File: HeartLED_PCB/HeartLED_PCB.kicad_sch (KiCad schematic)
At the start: 36 parts, among them U1 ICM7555CBAZ, U2 CD4017BM, U3 HT7750A, U4 HX SS12F44G4

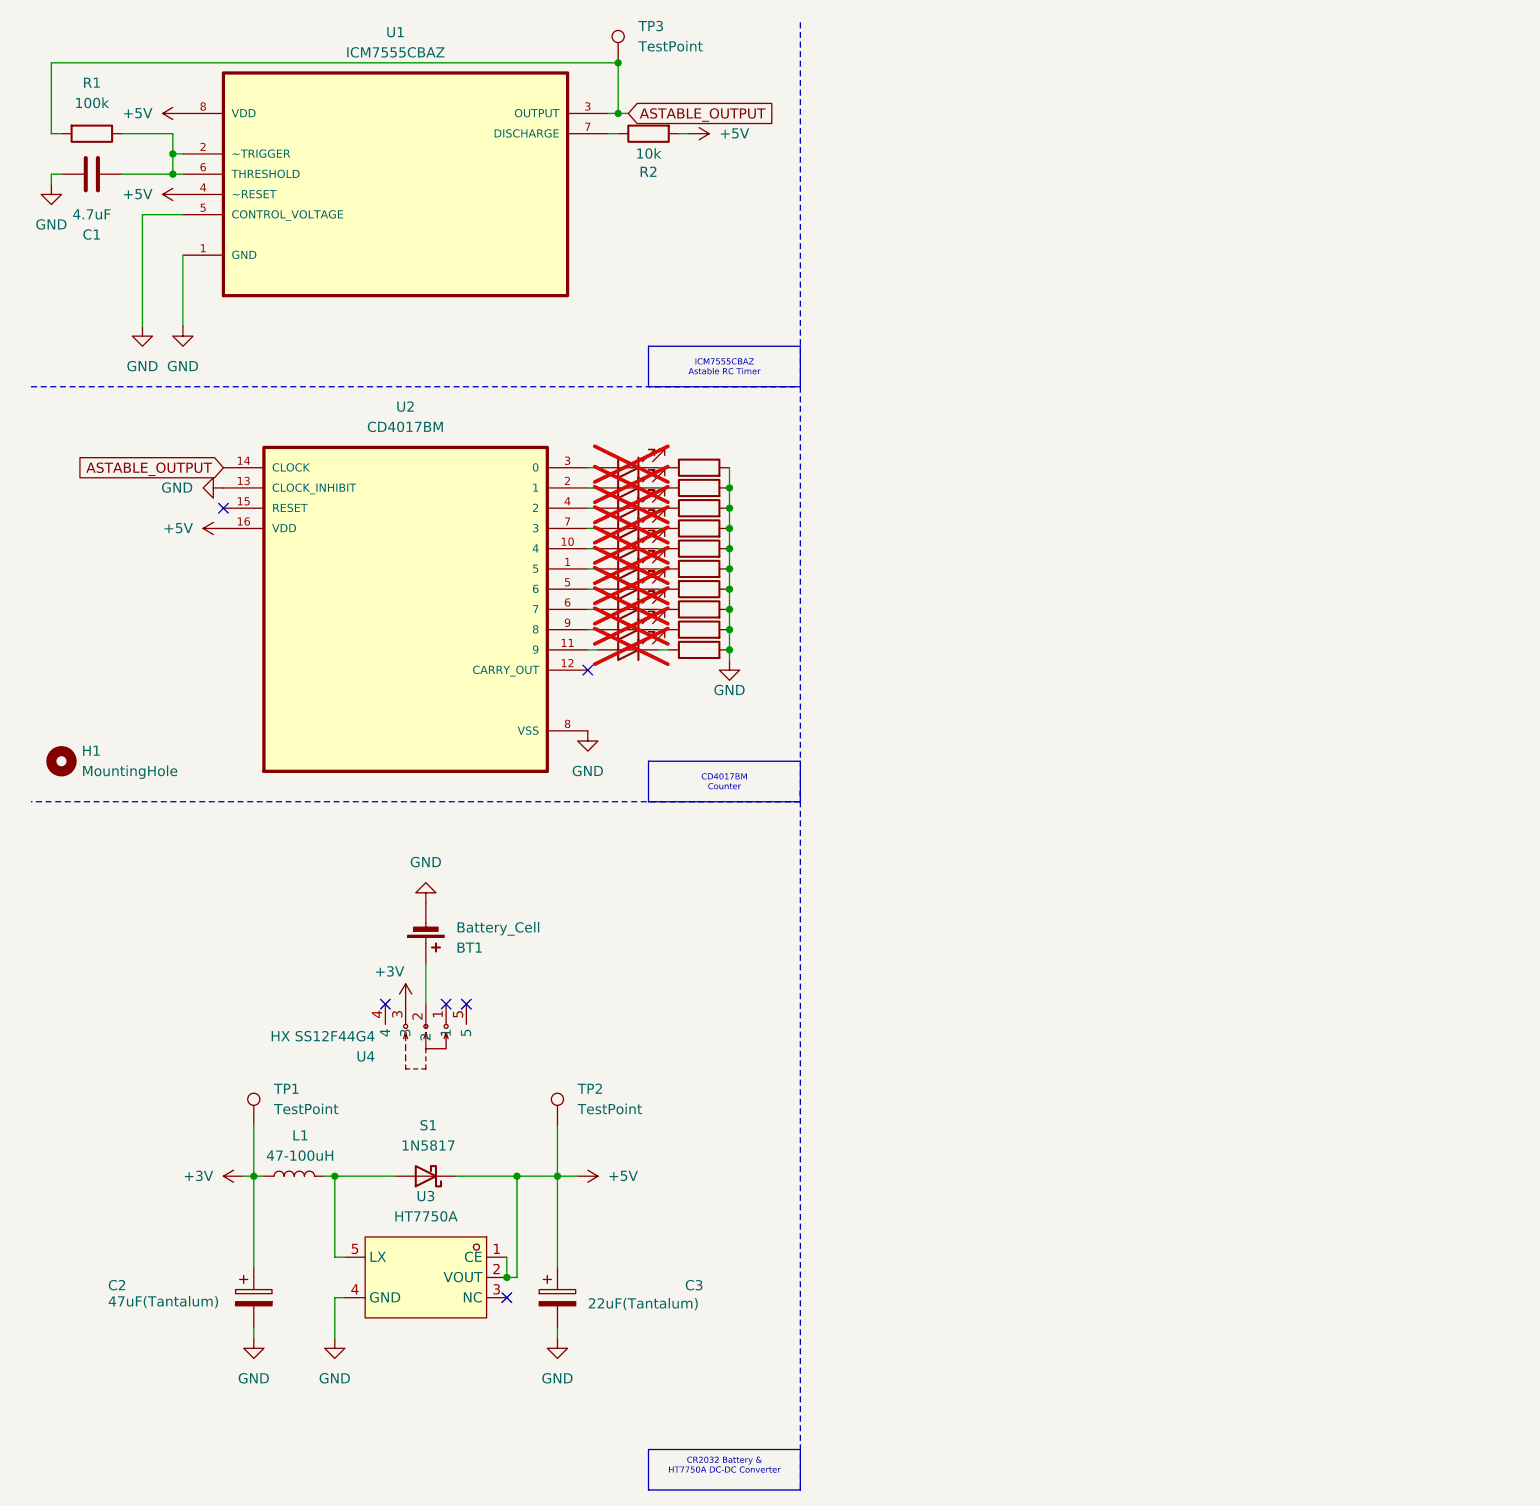
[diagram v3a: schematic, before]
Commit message: Changed Timer and Counter models
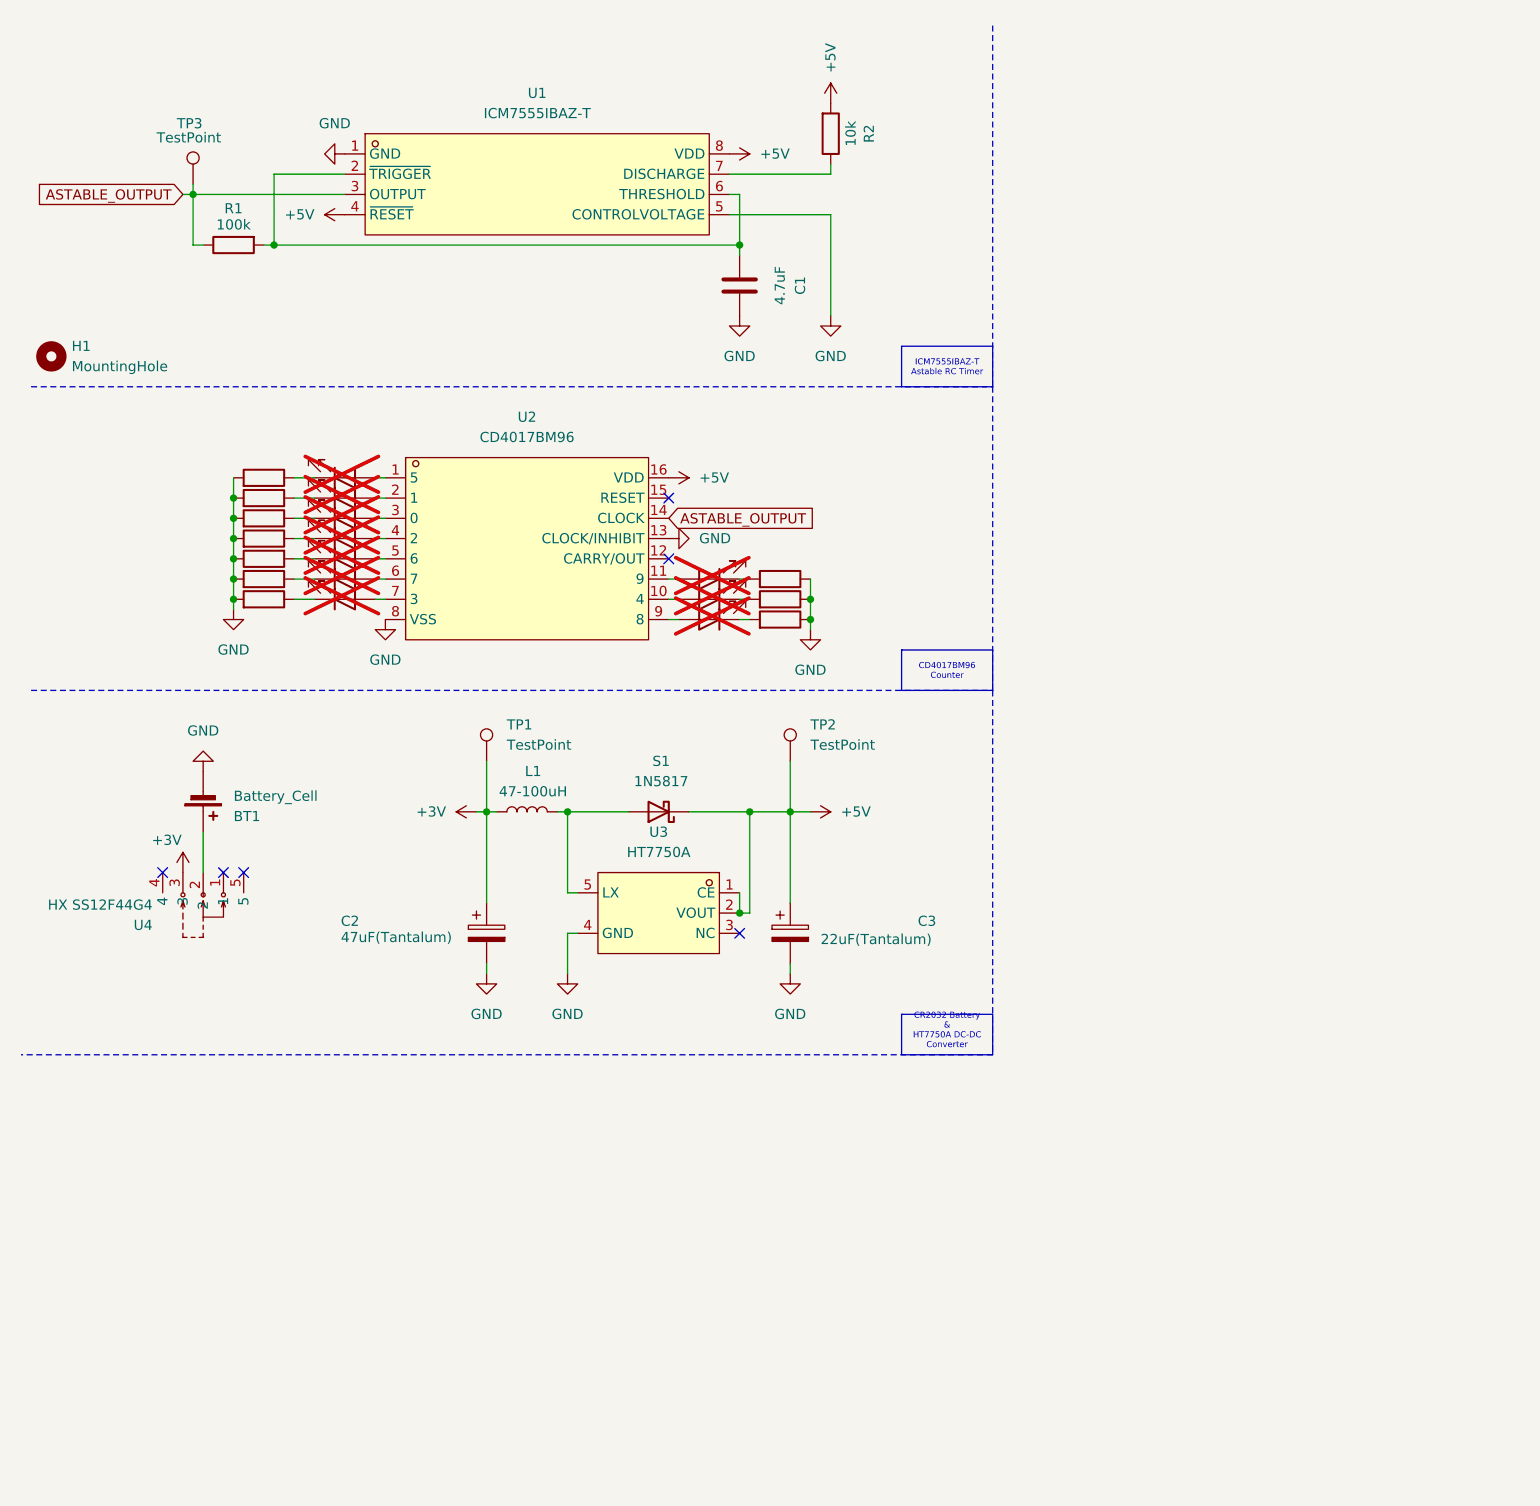
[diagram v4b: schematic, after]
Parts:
- removed U1: ICM7555CBAZ, FOOTPRINTS:ICM7555CBAZ, symbol ICM7555CBAZ:ICM7555CBAZ
- removed U2: CD4017BM, FOOTPRINTS:CD4017BM, symbol CD4017BM:CD4017BM
- added U1: ICM7555IBAZ-T, FOOTPRINTS:ICM7555IBAZ-T, symbol ICM7555IBAZ-T:ICM7555IBAZ-T
- added U2: CD4017BM96, FOOTPRINTS:CD4017BM96, symbol CD4017BM96:CD4017BM96
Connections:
- net +5V: now also U1.4 (~{RESET}), U1.8 (VDD), U2.16 (VDD)
- net ASTABLE_OUTPUT: now also R1.1, U1.3 (OUTPUT), U2.14 (CLOCK); no longer R1.2
- net GND: now also R10.1, R11.1, R12.1, U1.1 (GND), U1.5 (CONTROLVOLTAGE), U2.13 (CLOCK/INHIBIT), U2.8 (VSS); no longer R10.2, R11.2, R12.2
- net at D9.1 (K): now also R11.2; no longer R11.1
- net at D10.1 (K): now also R12.2; no longer R12.1
- net at D8.1 (K): now also R10.2; no longer R10.1
- net at D1.2 (A): now also U2.1 (5)
- net at D10.2 (A): now also U2.11 (9)
- net at C1.1: now also R1.2, U1.2 (~{TRIGGER}), U1.6 (THRESHOLD); no longer R1.1
- net at R2.1: now also U1.7 (DISCHARGE)
- net at D3.2 (A): now also U2.3 (0)
- net at D8.2 (A): now also U2.9 (8)
- net at D9.2 (A): now also U2.10 (4)
- net at D2.2 (A): now also U2.2 (1)
- net at D4.2 (A): now also U2.4 (2)
- net at D5.2 (A): now also U2.5 (6)
- net at D6.2 (A): now also U2.6 (7)
- net at D7.2 (A): now also U2.7 (3)
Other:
- moved on the sheet: BT1, C1, C2, C3, H1, L1, R1, R2, S1, TP1, TP2, TP3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

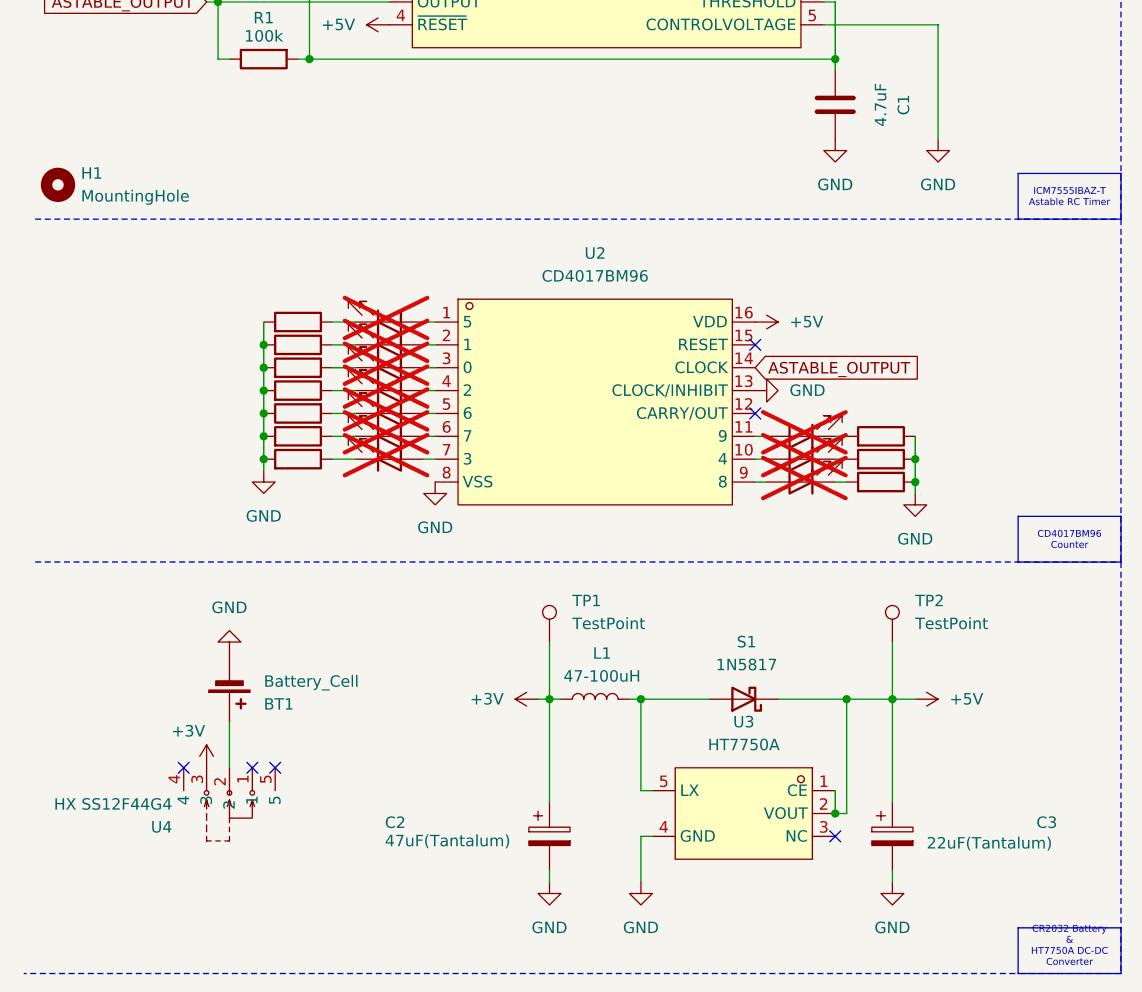
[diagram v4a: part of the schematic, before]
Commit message: Changed DC-DC Boost Converter
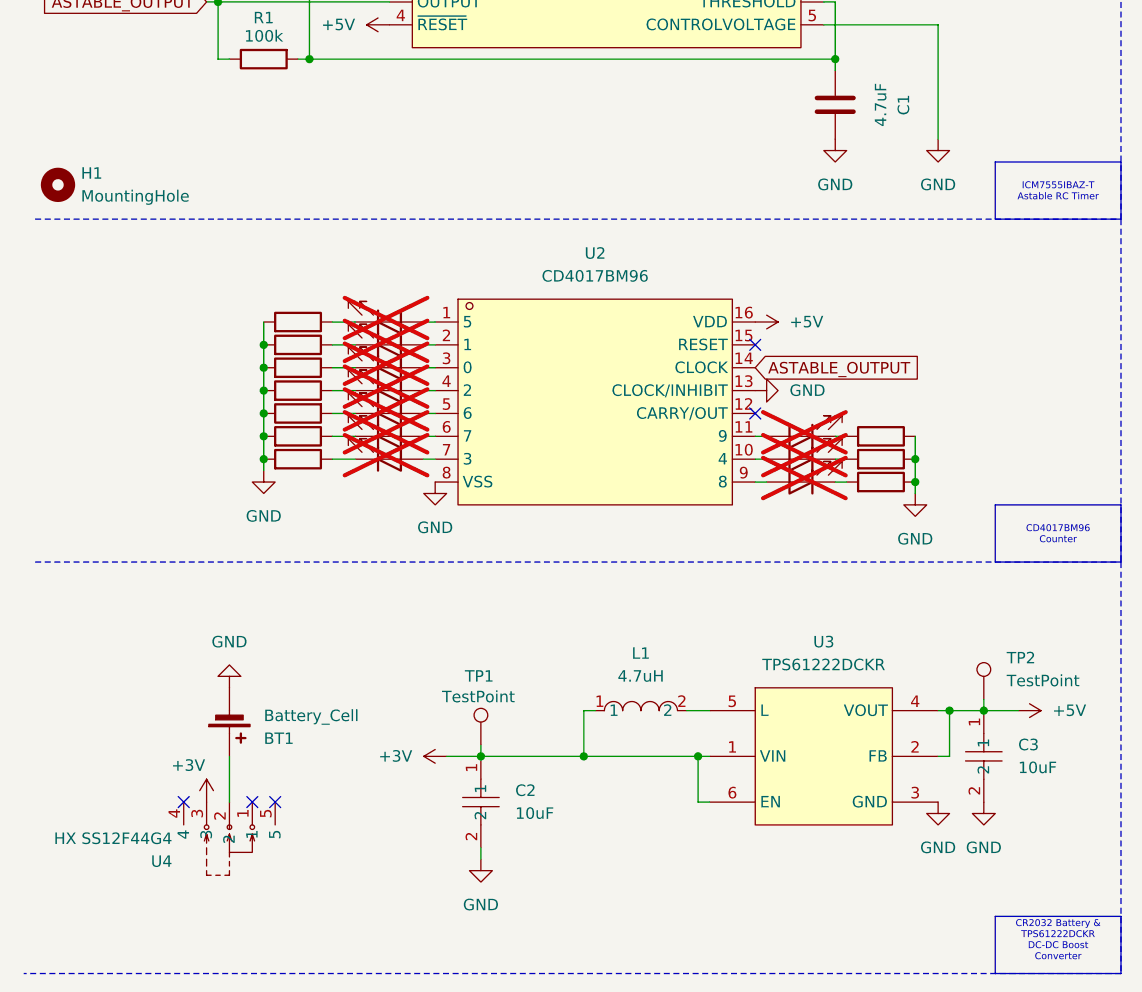
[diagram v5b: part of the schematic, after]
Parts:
- removed C2: 47uF(Tantalum), FOOTPRINTS:TAJA476K006RNJ, symbol Device:C_Polarized
- removed C3: 22uF(Tantalum), FOOTPRINTS:TAJA226M010RNJ, symbol Device:C_Polarized
- removed L1: 47-100uH, FOOTPRINTS:SMNR5040-470MT, symbol Device:L
- removed S1: 1N5817, FOOTPRINTS:1N5817W, symbol Diode:1N5817
- removed U3: HT7750A, FOOTPRINTS:HT7750A, symbol HT7750A:HT7750A_C259884
- added C2, C3: 10uF, FOOTPRINTS:CL10A106MQ8NNNC, symbol CL10A106MQ8NNNC:CL10A106MQ8NNNC
- added L1: 4.7uH, FOOTPRINTS:LQH3NPN4R7MMEL, symbol LQH3NPN4R7MMEL:LQH3NPN4R7MMEL
- added U3: TPS61222DCKR, FOOTPRINTS:TPS61222DCKR, symbol TPS61222DCKR:TPS61222DCKR
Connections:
- net +3V: now also C2.1, L1.1, U3.1 (VIN), U3.6 (EN)
- net +5V: now also C3.1, U3.2 (FB), U3.4 (VOUT)
- net GND: now also C2.2, C3.2, U3.3 (GND)
- new net: L1.2, U3.5 (L)
- no-connect marks 6 -> 5
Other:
- moved on the sheet: BT1, TP1, TP2, U4

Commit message: Routing done
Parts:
- removed BT1: Battery_Cell, Battery:BatteryHolder_Keystone_1060_1x2032, symbol Device:Battery_Cell
- removed C1: 4.7uF, FOOTPRINTS:CL10A475KP8NNNC, symbol Device:C
- removed C2, C3: 10uF, FOOTPRINTS:CL10A106MQ8NNNC, symbol CL10A106MQ8NNNC:CL10A106MQ8NNNC
- removed L1: 4.7uH, FOOTPRINTS:LQH3NPN4R7MMEL, symbol LQH3NPN4R7MMEL:LQH3NPN4R7MMEL
- removed TP1, TP2, TP3: TestPoint, TestPoint:TestPoint_Pad_D1.0mm, symbol Connector:TestPoint
- removed U1: ICM7555IBAZ-T, FOOTPRINTS:ICM7555IBAZ-T, symbol ICM7555IBAZ-T:ICM7555IBAZ-T
- removed U2: CD4017BM96, FOOTPRINTS:CD4017BM96, symbol CD4017BM96:CD4017BM96
- removed U3: TPS61222DCKR, FOOTPRINTS:TPS61222DCKR, symbol TPS61222DCKR:TPS61222DCKR
- removed U4: HX SS12F44G4, FOOTPRINTS:HX SS12F44G4, symbol HXSS12F44G4:HXSS12F44G4
- added C1: 47uF, Capacitor_THT:C_Radial_D5.0mm_H7.0mm_P2.00mm, symbol Device:C_Polarized
- added SW1: SS12D00G3, FOOTPRINTS:SS12D00G3, symbol SS12D00G3:SS12D00G3
- added U1: NE555DR, FOOTPRINTS:NE555DR, symbol NE555DR:NE555DR
- added U2: 1066, FOOTPRINTS:1066, symbol 1066:1066
- D1, D10, D2, D3, D4, D5, D6, D7, D8, D9: now fitted
- H1: footprint MountingHole:MountingHole_2.1mm -> MountingHole:MountingHole_3.2mm_M3
- R1: value 100k -> 1k; footprint FOOTPRINTS:0603WAJ0104T5E -> Resistor_THT:R_Axial_DIN0207_L6.3mm_D2.5mm_P7.62mm_Horizontal; LCSC C15458 -> (none)
- R10, R3, R4, R5, R6, R7, R8, R9: value 3.3k -> 1k; footprint FOOTPRINTS:0402WGJ0332TCE -> Resistor_THT:R_Axial_DIN0207_L6.3mm_D2.5mm_P7.62mm_Horizontal; LCSC C25936 -> (none)
- R11: value 3.3k -> 10K; footprint FOOTPRINTS:0402WGJ0332TCE -> Resistor_THT:R_Axial_DIN0207_L6.3mm_D2.5mm_P7.62mm_Horizontal; LCSC C25936 -> (none)
- R12: value 3.3k -> 1OK; footprint FOOTPRINTS:0402WGJ0332TCE -> Resistor_THT:R_Axial_DIN0207_L6.3mm_D2.5mm_P7.62mm_Horizontal; LCSC C25936 -> (none)
- R2: value 10k -> 1k; footprint FOOTPRINTS:0402WGJ0103TCE -> Resistor_THT:R_Axial_DIN0207_L6.3mm_D2.5mm_P7.62mm_Horizontal; LCSC C25531 -> (none)
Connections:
- net +5V is gone; now on an unnamed net: R2.2
- net ASTABLE_OUTPUT is gone; now on an unnamed net: R1.1
- net GND: now also D10.1 (K), D6.1 (K), D7.1 (K), D8.1 (K), D9.1 (K), C1.2, U1.1 (GND), U2.1; no longer R10.1, R11.1, R12.1, R3.2, R4.2, R5.2, R6.2, R7.1, R8.2, R9.2
- net VCC: now reaches D1.2 (A)
- net VCC: now also D2.2 (A), D3.2 (A), D4.2 (A), D5.2 (A), R12.1, SW1.3, U1.4 (RST), U1.8 (VCC)
- net at D9.2 (A): now also R9.2
- net at D10.2 (A): now also R10.2
- net at D6.2 (A): now also R6.2
- net at D7.2 (A): now also R7.2
- net at D8.2 (A): now also R8.2
- net at R8.1: now also R1.2, R10.1, R3.2, R4.2, R5.2, R6.1, R7.1, R9.1, U1.3 (OUT); no longer D6.1 (K)
- net at D1.1 (K): no longer R3.1
- net at D3.1 (K): now also R3.1; no longer R5.1
- net at R12.2: now also R11.1, U1.7 (DISCH); no longer D10.1 (K)
- net at R11.2: now also C1.1, U1.2 (TRIG), U1.6 (THRES); no longer D9.1 (K)
- net at D5.1 (K): now also R5.1; no longer R7.2
- net at R4.1: now also D4.1 (K); no longer D2.1 (K)
- net at R2.1: now also D2.1 (K)
- new net: SW1.2, U2.2
- no-connect marks 5 -> 2

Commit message: Added silkscreen logos
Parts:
- H1: footprint MountingHole:MountingHole_3.2mm_M3 -> MountingHole:MountingHole_2.7mm
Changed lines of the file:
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@@
 			)
 		)
-		(property "Footprint" "MountingHole:MountingHole_3.2mm_M3"
+		(property "Footprint" "MountingHole:MountingHole_2.7mm"
 			(at 82.55 114.3 0)
 			(effects
